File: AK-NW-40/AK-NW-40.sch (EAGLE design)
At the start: 4 parts, among them J1 POWER_JACK-SLOTS

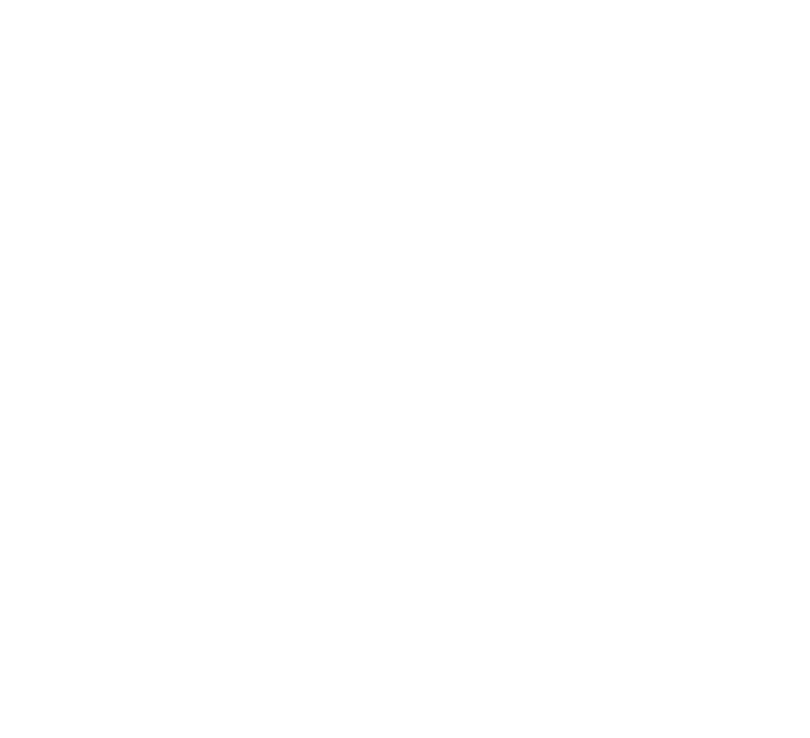
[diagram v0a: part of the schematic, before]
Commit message: Fixed hole positions based on drawings provided by SZOMK.
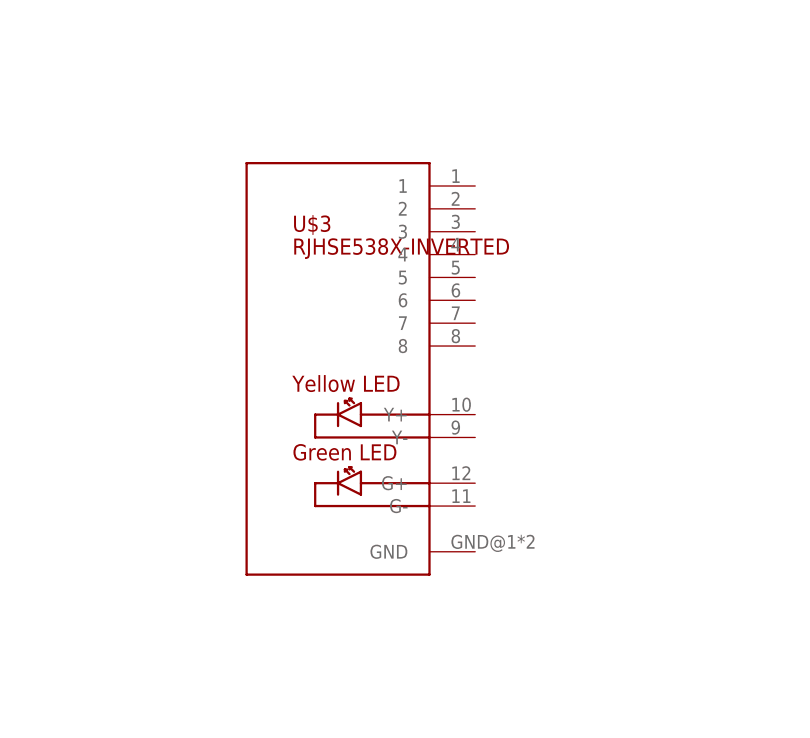
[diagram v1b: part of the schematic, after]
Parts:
- added U$3: RJHSE538X-INVERTED, SuperHouse-Connectors:RJHSE538X-INVERTED
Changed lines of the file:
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@@
 <part name="J1" library="SuperHouse-Connectors" library_urn="urn:adsk.eagle:library:11765989" deviceset="POWER_JACK" device="-SLOTS" package3d_urn="urn:adsk.eagle:package:7066536/4"/>
 <part name="U$2" library="SuperHouse-Switches" library_urn="urn:adsk.eagle:library:11744182" deviceset="TAC-SWITCH-2PIN-GND" device="-FSMMSHPTR" package3d_urn="urn:adsk.eagle:package:11818000/1"/>
+<part name="U$3" library="SuperHouse-Connectors" library_urn="urn:adsk.eagle:library:11765989" deviceset="RJHSE538X" device="-INVERTED" package3d_urn="urn:adsk.eagle:package:30747766/3"/>
 </parts>
 <sheets>
@@
 <attribute name="VALUE" x="35.56" y="95.25" size="1.778" layer="96"/>
 </instance>
+<instance part="U$3" gate="G$1" x="137.16" y="109.22" smashed="yes">
+<attribute name="NAME" x="132.08" y="124.46" size="1.778" layer="94"/>
+<attribute name="VALUE" x="132.08" y="121.92" size="1.778" layer="94"/>
+</instance>
 </instances>
